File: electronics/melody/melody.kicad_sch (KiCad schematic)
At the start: 47 parts, among them J1 USB_B, J2 Raspberry_Pi_4, J3 Conn_01x04_Pin, J4 Conn_01x01_Pin, J5 Conn_01x16_Pin, J6 Conn_01x16_Pin, SW1 SW_Push, SW2 SW_Push, SW3 SW_Push, SW4 SW_Push, SW5 SW_Push, SW6 SW_Push, SW7 SW_Push, U1 74154, U2 74154

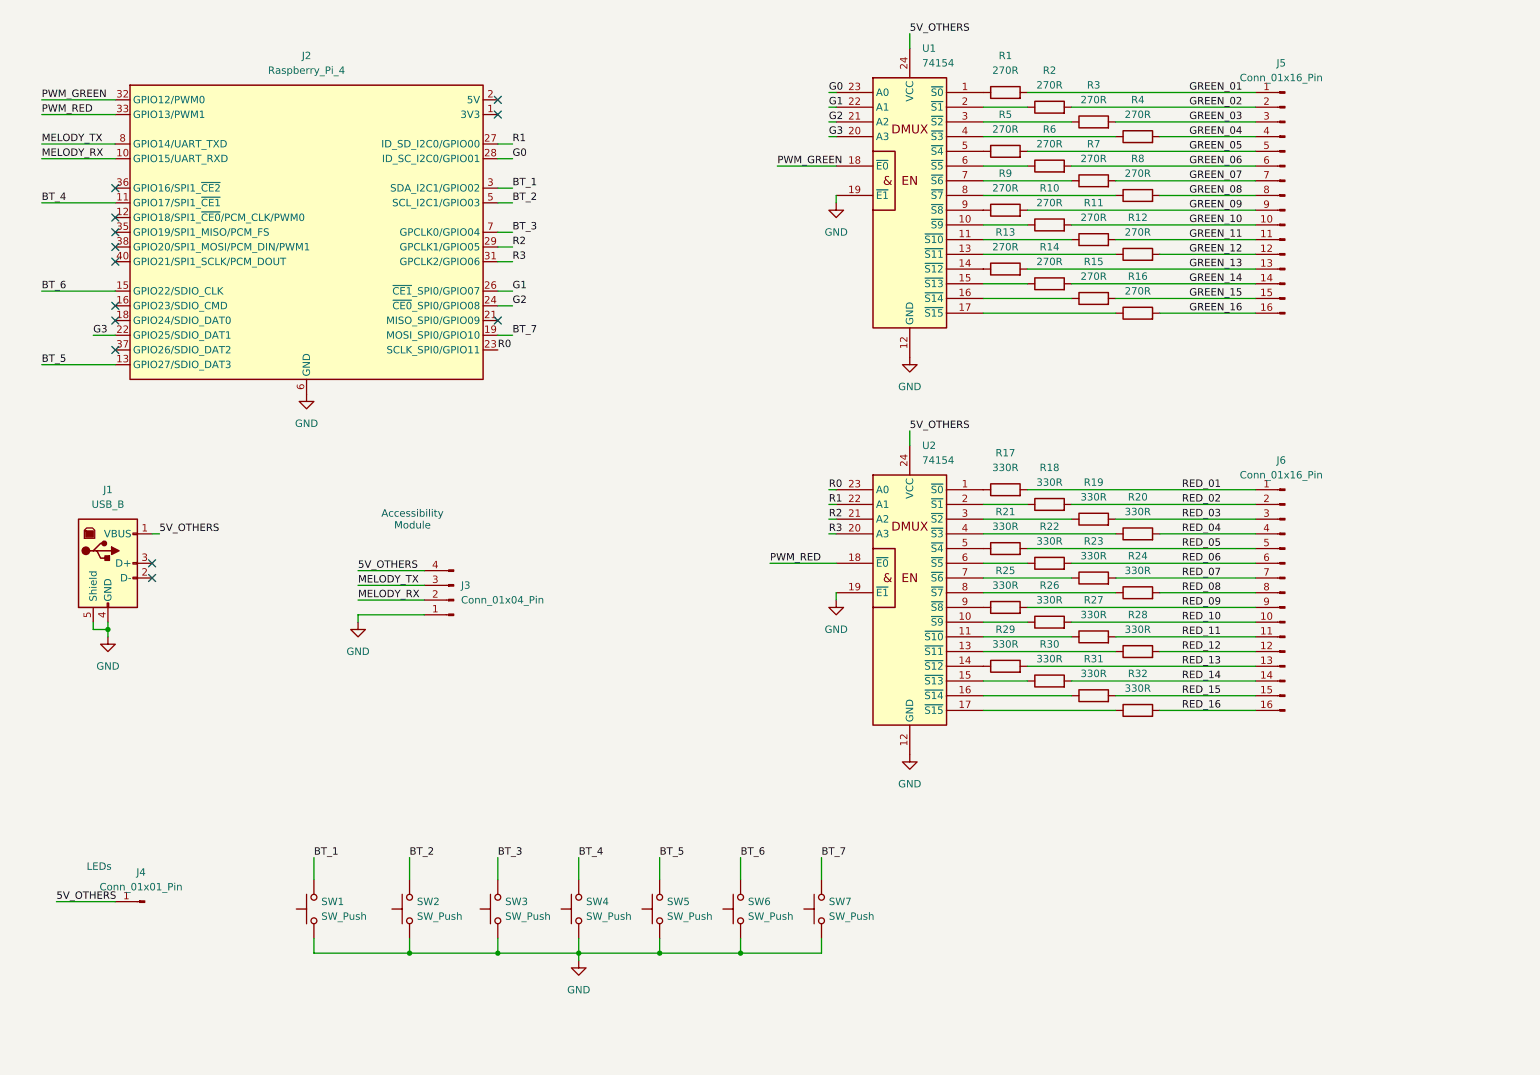
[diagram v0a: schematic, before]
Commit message: change IC 74->40 + shared power supply for processors + PCB
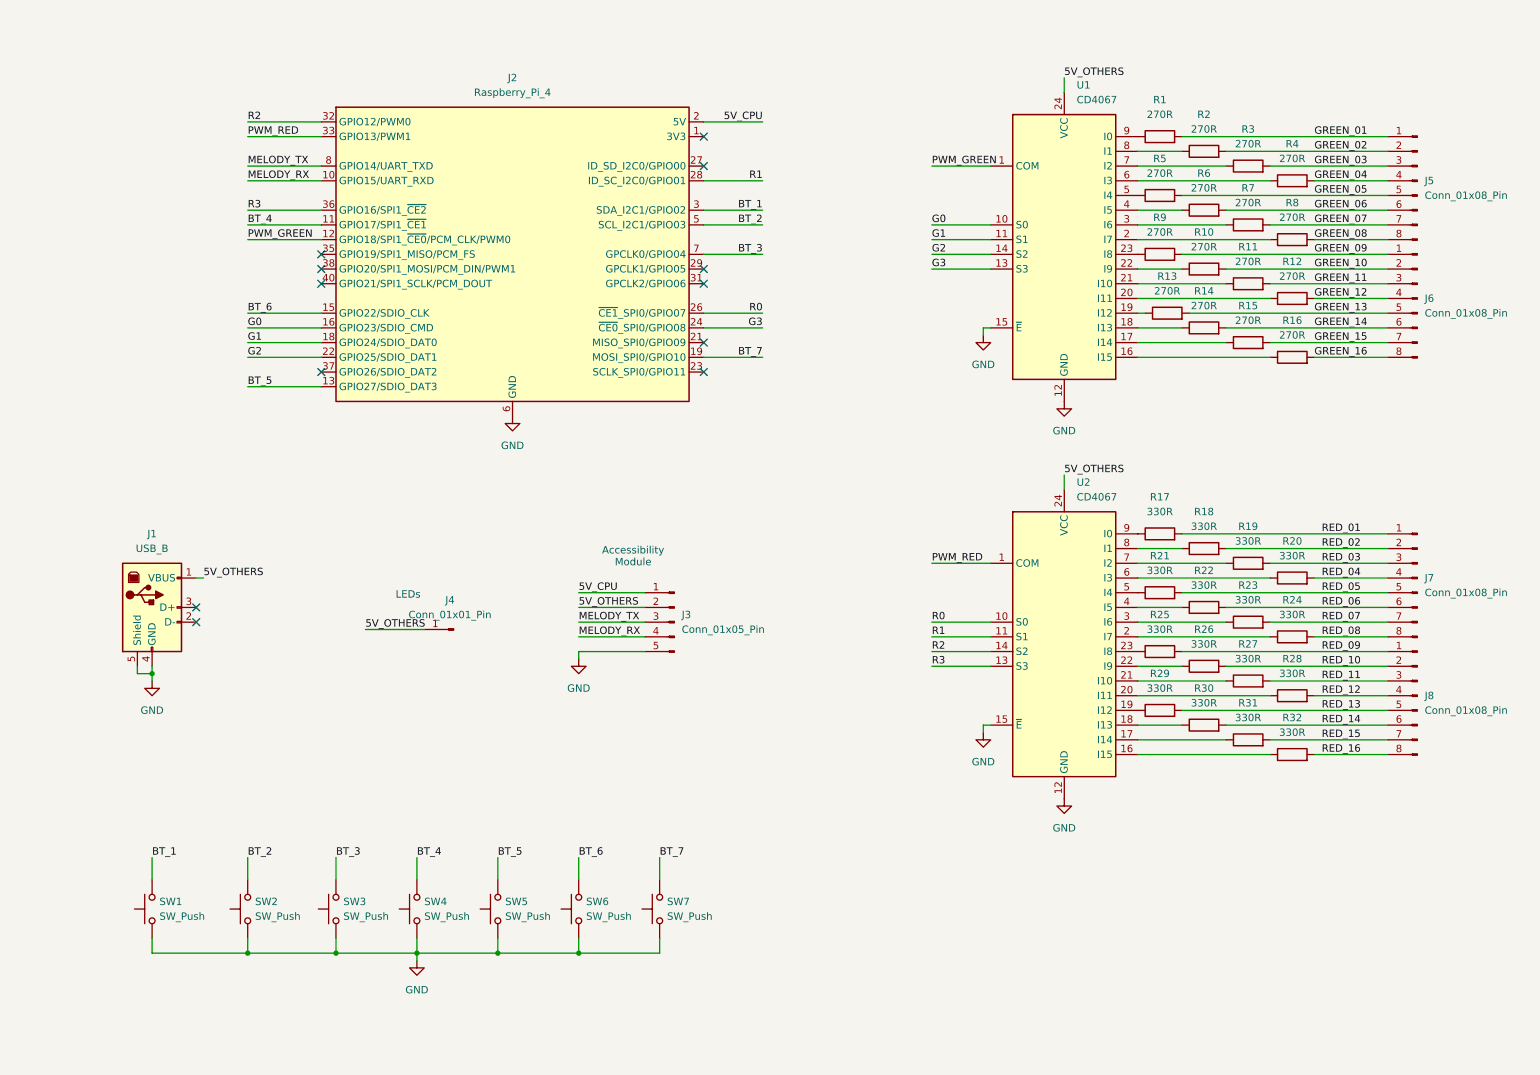
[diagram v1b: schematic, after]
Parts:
- removed J3: Conn_01x04_Pin, Connector_PinSocket_2.54mm:PinSocket_1x04_P2.54mm_Vertical, symbol Connector:Conn_01x04_Pin
- removed J5, J6: Conn_01x16_Pin, Connector_PinSocket_2.54mm:PinSocket_1x16_P2.54mm_Vertical, symbol Connector:Conn_01x16_Pin
- removed U1, U2: 74154, Package_DIP:DIP-24_W15.24mm_Socket_LongPads, symbol 74xx_IEEE:74154
- added J3: Conn_01x05_Pin, Connector_PinHeader_2.54mm:PinHeader_1x05_P2.54mm_Vertical, symbol Connector:Conn_01x05_Pin
- added J5, J6, J7, J8: Conn_01x08_Pin, Connector_PinHeader_2.54mm:PinHeader_1x08_P2.54mm_Vertical, symbol Connector:Conn_01x08_Pin
- added U1, U2: CD4067, Package_DIP:DIP-24_W15.24mm_LongPads, symbol 74xx:CD74HC4067M
- R1, R10, R11, R12, R13, R14, R15, R16, R17, R18, R19, R2, R20, R21, R22, R23, R24, R25, R26, R27, R28, R29, R3, R30, R31, R32, R4, R5, R6, R7, R8, R9: footprint (none) -> Resistor_THT:R_Axial_DIN0204_L3.6mm_D1.6mm_P7.62mm_Horizontal
- SW1, SW2, SW3, SW4, SW5, SW6, SW7: footprint (none) -> Connector_PinHeader_2.54mm:PinHeader_1x02_P2.54mm_Vertical
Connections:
- net 5V_OTHERS: now also J3.2 (Pin_2), U1.24 (VCC), U2.24 (VCC)
- net G0: now also J2.16 (GPIO23/SDIO_CMD), U1.10 (S0); no longer J2.28 (ID_SC_I2C0/GPIO01)
- net G1: now also J2.18 (GPIO24/SDIO_DAT0), U1.11 (S1); no longer J2.26 (~{CE1}_SPI0/GPIO07)
- net G2: now also J2.22 (GPIO25/SDIO_DAT1), U1.14 (S2); no longer J2.24 (~{CE0}_SPI0/GPIO08)
- net G3: now also J2.24 (~{CE0}_SPI0/GPIO08), U1.13 (S3); no longer J2.22 (GPIO25/SDIO_DAT1)
- net GND: now also J3.5 (Pin_5), U1.12 (GND), U1.15 (~{E}), U2.12 (GND), U2.15 (~{E})
- net GREEN_01: now also J5.1 (Pin_1)
- net GREEN_02: now also J5.2 (Pin_2)
- net GREEN_03: now also J5.3 (Pin_3)
- net GREEN_04: now also J5.4 (Pin_4)
- net GREEN_05: now also J5.5 (Pin_5)
- net GREEN_06: now also J5.6 (Pin_6)
- net GREEN_07: now also J5.7 (Pin_7)
- net GREEN_08: now also J5.8 (Pin_8)
- net GREEN_09: now also J6.1 (Pin_1)
- net GREEN_10: now also J6.2 (Pin_2)
- net GREEN_11: now also J6.3 (Pin_3)
- net GREEN_12: now also J6.4 (Pin_4)
- net GREEN_13: now also J6.5 (Pin_5)
- net GREEN_14: now also J6.6 (Pin_6)
- net GREEN_15: now also J6.7 (Pin_7)
- net GREEN_16: now also J6.8 (Pin_8)
- net MELODY_RX: now also J3.4 (Pin_4)
- net MELODY_TX: now also J3.3 (Pin_3)
- net PWM_GREEN: now also J2.12 (GPIO18/SPI1_~{CE0}/PCM_CLK/PWM0), U1.1 (COM); no longer J2.32 (GPIO12/PWM0)
- net PWM_RED: now also U2.1 (COM)
- net R0: now also J2.26 (~{CE1}_SPI0/GPIO07), U2.10 (S0); no longer J2.23 (SCLK_SPI0/GPIO11)
- net R1: now also J2.28 (ID_SC_I2C0/GPIO01), U2.11 (S1); no longer J2.27 (ID_SD_I2C0/GPIO00)
- net R2: now also J2.32 (GPIO12/PWM0), U2.14 (S2); no longer J2.29 (GPCLK1/GPIO05)
- net R3: now also J2.36 (GPIO16/SPI1_~{CE2}), U2.13 (S3); no longer J2.31 (GPCLK2/GPIO06)
- net RED_01: now also J7.1 (Pin_1)
- net RED_02: now also J7.2 (Pin_2)
- net RED_03: now also J7.3 (Pin_3)
- net RED_04: now also J7.4 (Pin_4)
- net RED_05: now also J7.5 (Pin_5)
- net RED_06: now also J7.6 (Pin_6)
- net RED_07: now also J7.7 (Pin_7)
- net RED_08: now also J7.8 (Pin_8)
- net RED_09: now also J8.1 (Pin_1)
- net RED_10: now also J8.2 (Pin_2)
- net RED_11: now also J8.3 (Pin_3)
- net RED_12: now also J8.4 (Pin_4)
- net RED_13: now also J8.5 (Pin_5)
- net RED_14: now also J8.6 (Pin_6)
- net RED_15: now also J8.7 (Pin_7)
- net RED_16: now also J8.8 (Pin_8)
- net at R29.1: now also U2.19 (I12)
- net at R17.1: now also U2.9 (I0)
- net at R20.1: now also U2.6 (I3)
- net at R30.1: now also U2.18 (I13)
- net at R26.1: now also U2.22 (I9)
- net at R25.1: now also U2.23 (I8)
- net at R21.1: now also U2.5 (I4)
- net at R1.1: now also U1.9 (I0)
- net at R27.1: now also U2.21 (I10)
- net at R28.1: now also U2.20 (I11)
- net at R31.1: now also U2.17 (I14)
- net at R32.1: now also U2.16 (I15)
- net at R18.1: now also U2.8 (I1)
- net at R19.1: now also U2.7 (I2)
- net at R22.1: now also U2.4 (I5)
- net at R23.1: now also U2.3 (I6)
- net at R24.1: now also U2.2 (I7)
- net at R6.1: now also U1.4 (I5)
- net at R13.1: now also U1.19 (I12)
- net at R14.1: now also U1.18 (I13)
- net at R4.1: now also U1.6 (I3)
- net at R5.1: now also U1.5 (I4)
- net at R2.1: now also U1.8 (I1)
- net at R15.1: now also U1.17 (I14)
- net at R3.1: now also U1.7 (I2)
- net at R16.1: now also U1.16 (I15)
- net at R7.1: now also U1.3 (I6)
- net at R11.1: now also U1.21 (I10)
- net at R10.1: now also U1.22 (I9)
- net at R9.1: now also U1.23 (I8)
- net at R12.1: now also U1.20 (I11)
- net at R8.1: now also U1.2 (I7)
- net 5V_CPU: now reaches J2.2 (5V), J2.4 (5V)
- net 5V_CPU: now also J3.1 (Pin_1)
- no-connect marks 13 -> 12
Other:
- company: (none) -> UTFPR
- title: (none) -> Melody
- moved on the sheet: J1, J2, J4, R1, R10, R11, R12, R13, R14, R15, R16, R17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

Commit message: Melody schematic update
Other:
- note added: "Interface Buttons"
- moved on the sheet: J1, J2, J3, J4, SW1, SW2, SW3, SW4, SW5, SW6, SW7

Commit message: Atualização esquemático eletrônico
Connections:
- net R0 renamed S_R0
- net R1 renamed S_R1
- net R2 renamed S_R2
- net R3 renamed S_R3
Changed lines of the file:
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@@
 		)
 	)
-	(label "R2"
+	(label "S_R2"
 		(at 180.34 125.73 0)
 		(effects
@@
 		)
 	)
-	(label "R0"
+	(label "S_R0"
 		(at 140.97 100.33 180)
 		(effects
@@
 		)
 	)
-	(label "R1"
+	(label "S_R1"
 		(at 180.34 123.19 0)
 		(effects
@@
 		)
 	)
-	(label "R0"
+	(label "S_R0"
 		(at 180.34 120.65 0)
 		(effects
@@
 		)
 	)
-	(label "R1"
+	(label "S_R1"
 		(at 140.97 77.47 180)
 		(effects
@@
 		)
 	)
-	(label "R2"
+	(label "S_R2"
 		(at 52.07 67.31 0)
 		(effects
@@
 		)
 	)
-	(label "R3"
+	(label "S_R3"
 		(at 52.07 82.55 0)
 		(effects
@@
 		)
 	)
-	(label "R3"
+	(label "S_R3"
 		(at 180.34 128.27 0)
 		(effects
